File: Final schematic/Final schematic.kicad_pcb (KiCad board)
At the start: 2 copper layers, 140 x 90 mm, 39 parts, among them J1 PJ-102AH, J2 Conn_01x06, J3 Conn_02x03_Odd_Even, SW1 Omron_B3F_SPST, SW2 Omron_B3F_SPST, SW3 Omron_B3F_SPST, SW4 Omron_B3F_SPST, U1 ATmega328-PU, U2 L7805, U3 MAX7219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

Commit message: PCB UPDATE
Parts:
- DS1: value LED_Display_1001 -> LED
- J1: value PJ-102AH -> Power_inlet_vertical; footprint footprints:PJ-102AH -> footprints:Wurth-694106402002; moved to B.Cu
- moved J1 21.0 mm to (187.3, 80.6), turned to 180 degrees
- moved C3 11.8 mm to (194.1, 73.2)
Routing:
- net Net-(C3-Pad1): track 8.03 -> 30.3 mm, vias 0 -> 1
- net VCC: track 54.3 -> 66.5 mm, vias 0 -> 11
- net GND: track 96.1 -> 92.1 mm, vias 20 -> 21

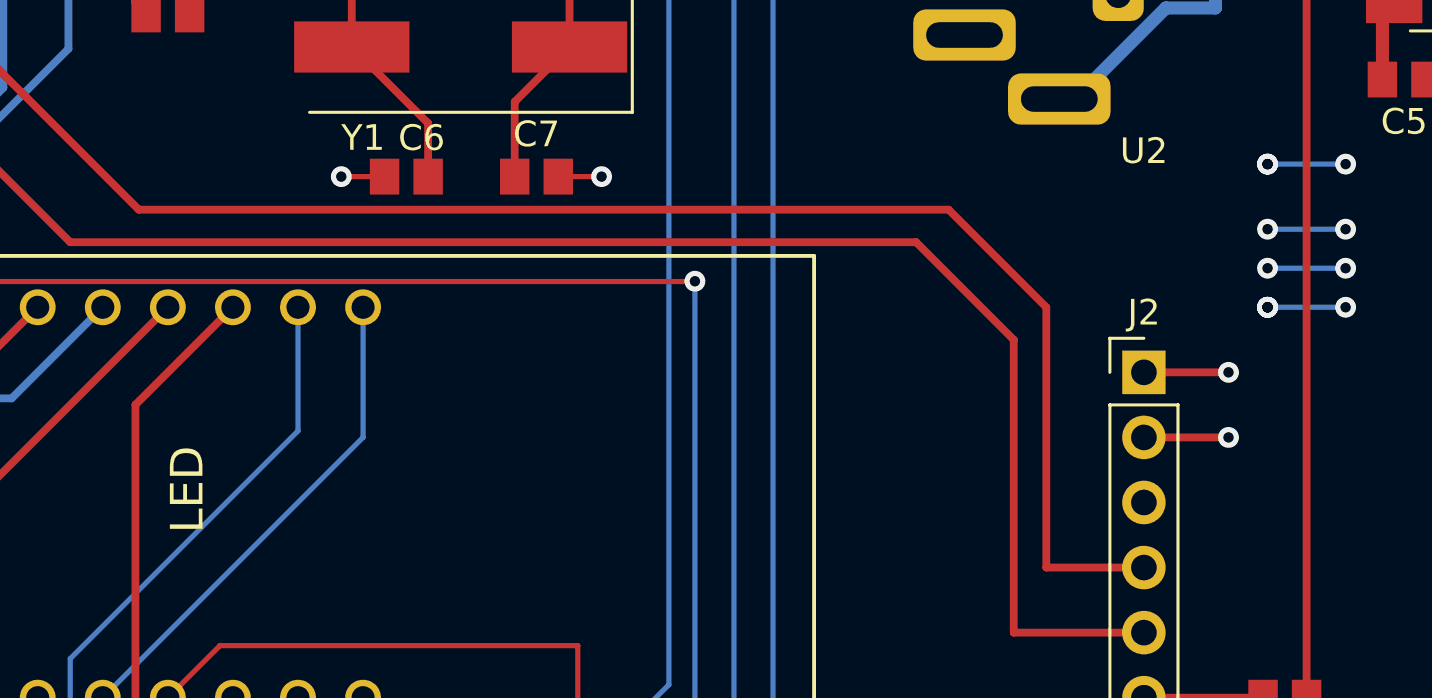
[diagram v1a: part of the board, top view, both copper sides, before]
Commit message: A few updates before manufacturing
Hi Ganiru, just fixing a few small things on the board and schematic before we send it for manufacturing.
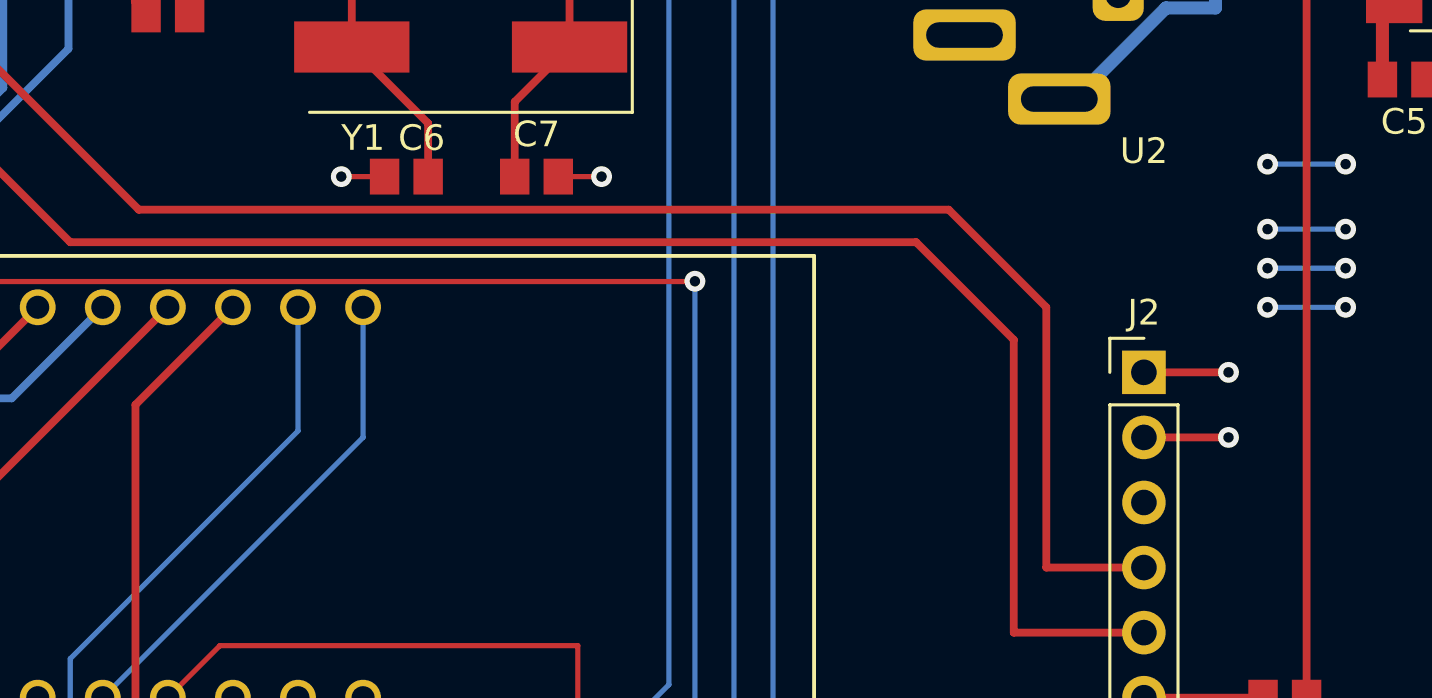
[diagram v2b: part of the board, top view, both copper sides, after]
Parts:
- DS1: value LED -> LED_Display_1001
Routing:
- net VCC: vias 11 -> 8
